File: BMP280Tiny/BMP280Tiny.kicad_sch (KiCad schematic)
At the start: 3 parts, among them J1 Programming Port, U1 ATtiny88-A, U2 AMS1117-5.0

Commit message: work on new vario board
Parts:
- removed U1: ATtiny88-A, Package_QFP:TQFP-32_7x7mm_P0.8mm, symbol MCU_Microchip_ATtiny:ATtiny88-A
- added C1: 0.1uF, Capacitor_SMD:C_0603_1608Metric_Pad1.08x0.95mm_HandSolder, symbol Device:C
- added J2: 9V Battery, Connector_Molex:Molex_KK-254_AE-6410-02A_1x02_P2.54mm_Vertical, symbol Connector_Generic:Conn_01x02
- added U1: ATtiny88-A, Package_QFP:TQFP-32_7x7mm_P0.8mm, symbol Project Library:ATtiny88-A
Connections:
- net GND: now reaches U2.1 (GND)
- net GND: now also C1.1, J2.1 (Pin_1)
- net 5V: now reaches U2.2 (VO)
- net at U2.3 (VI): now also C1.2, J2.2 (Pin_2)

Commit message: work on attiny88 board schematic
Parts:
- added C2, C3: 0.1uF, Capacitor_SMD:C_0603_1608Metric_Pad1.08x0.95mm_HandSolder, symbol Device:C
- added D1, D2: LED, symbol Device:LED
- added J3: Piezo Buzzer, Connector_Molex:Molex_KK-254_AE-6410-02A_1x02_P2.54mm_Vertical, symbol Connector_Generic:Conn_01x02
- added R1, R2, R3: R, symbol Device:R
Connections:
- net 5V: now also J1.2 (Pin_2), U1.18 (AVCC), U1.4 (VCC), C2.2, C3.2, R1.1
- net GND: now also J1.6 (Pin_6), U1.21 (GND), U1.5 (GND), C2.1, C3.1, D1.1 (K), D2.1 (K)
- net at U1.12 (PB0): now also R3.1
- net at U1.13 (PB1): now also J3.2 (Pin_2)
- net at U1.14 (PB2): now also J3.1 (Pin_1)
- net at U1.15 (PB3): now also J1.4 (Pin_4)
- net at U1.16 (PB4): now also J1.1 (Pin_1)
- net at U1.17 (PB5): now also J1.3 (Pin_3), R2.1
- net at U1.29 (~{RESET}/PC6): now also J1.5 (Pin_5), R1.2
- new net: D2.2 (A), R3.2
- new net: D1.2 (A), R2.2
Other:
- moved on the sheet: J1

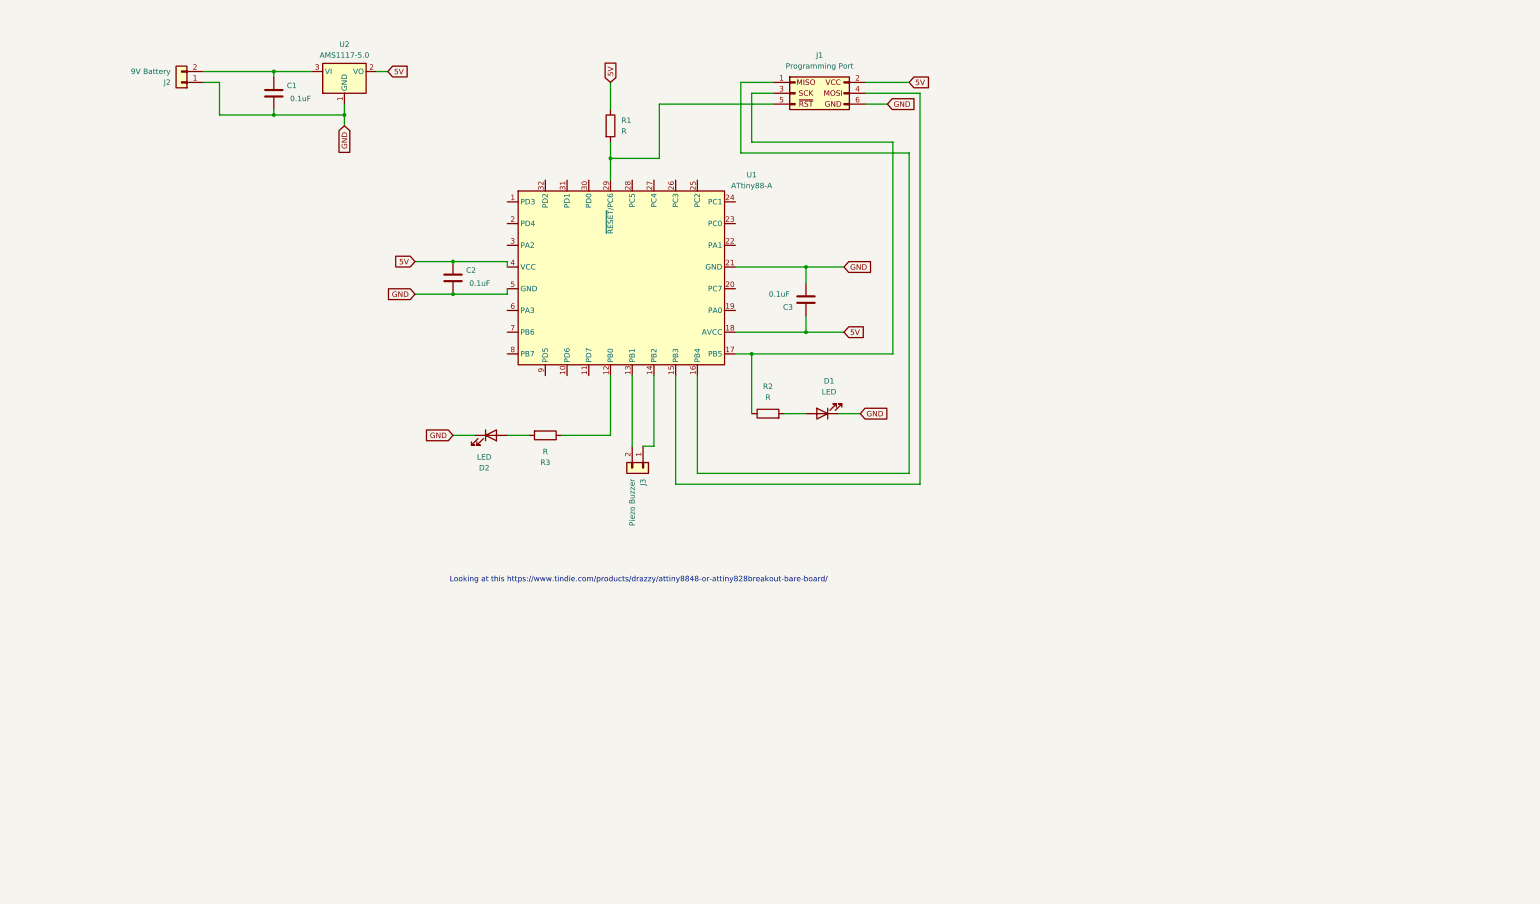
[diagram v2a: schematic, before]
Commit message: Vario v5 sent to jlcpcb for production
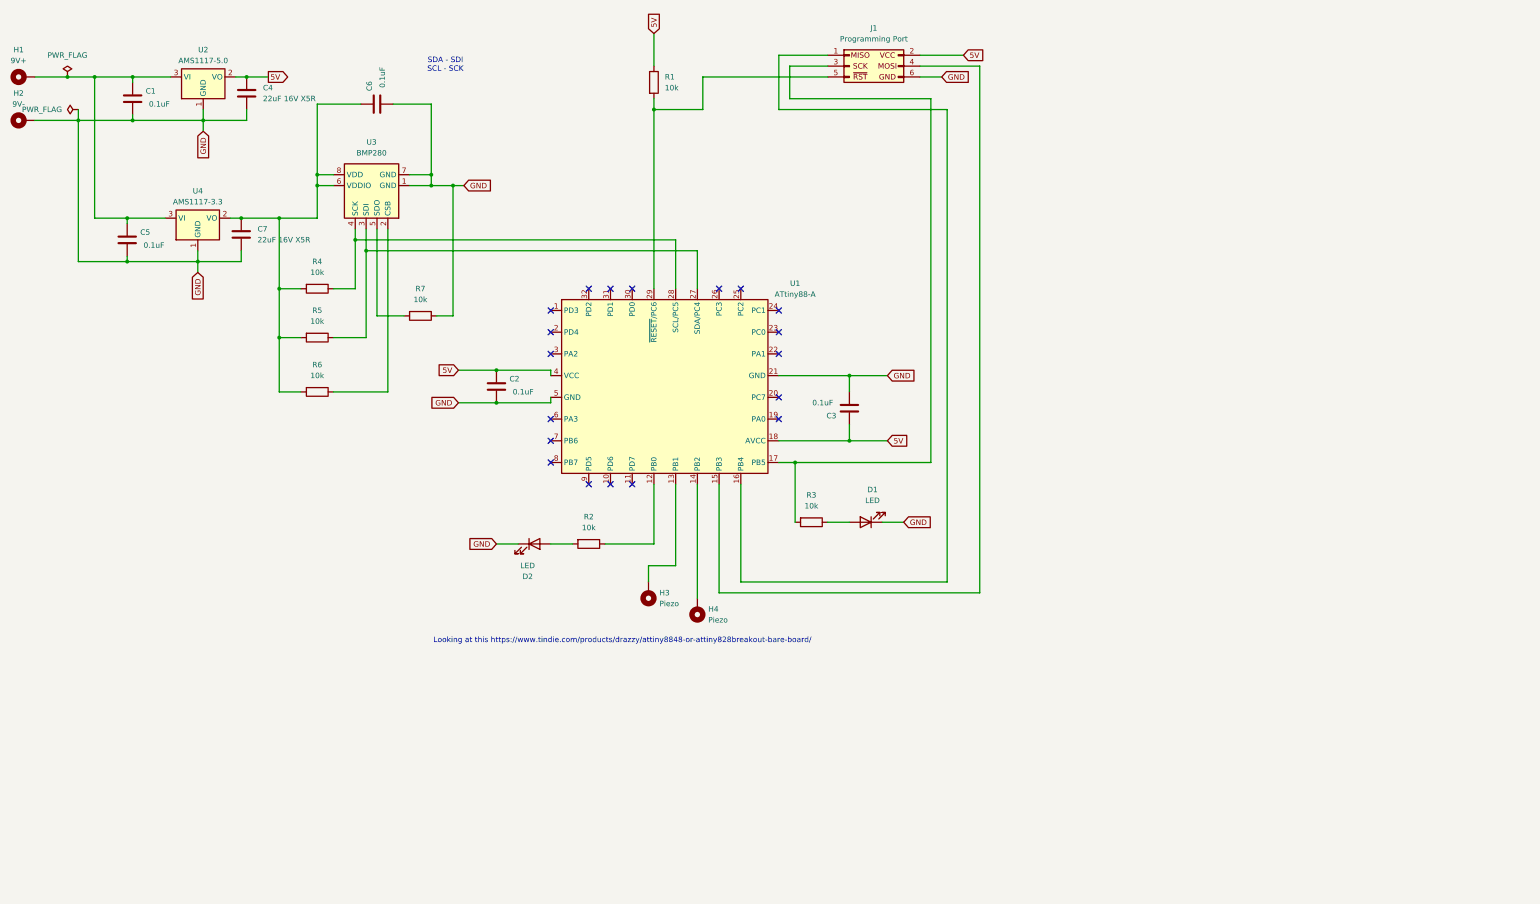
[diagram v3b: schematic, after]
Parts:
- removed J2: 9V Battery, Connector_Molex:Molex_KK-254_AE-6410-02A_1x02_P2.54mm_Vertical, symbol Connector_Generic:Conn_01x02
- removed J3: Piezo Buzzer, Connector_Molex:Molex_KK-254_AE-6410-02A_1x02_P2.54mm_Vertical, symbol Connector_Generic:Conn_01x02
- added C4, C7: 22uF 16V X5R, Capacitor_SMD:C_0805_2012Metric_Pad1.18x1.45mm_HandSolder, symbol Device:C
- added C5, C6: 0.1uF, Capacitor_SMD:C_0603_1608Metric_Pad1.08x0.95mm_HandSolder, symbol Device:C
- added H1: 9V+, TestPoint:TestPoint_THTPad_2.0x2.0mm_Drill1.0mm, symbol Mechanical:MountingHole_Pad
- added H2: 9V-, TestPoint:TestPoint_THTPad_2.0x2.0mm_Drill1.0mm, symbol Mechanical:MountingHole_Pad
- added H3, H4: Piezo, TestPoint:TestPoint_THTPad_2.0x2.0mm_Drill1.0mm, symbol Mechanical:MountingHole_Pad
- added R4, R5, R6, R7: 10k, Resistor_SMD:R_0603_1608Metric_Pad0.98x0.95mm_HandSolder, symbol Device:R
- added U3: BMP280, Library:Bosch_LGA-8_2x2.5mm_P0.65mm_ClockwisePinNumbering, symbol Sensor_Pressure:BMP280
- added U4: AMS1117-3.3, Package_TO_SOT_SMD:SOT-223-3_TabPin2, symbol Regulator_Linear:AMS1117-5.0
- D1, D2: footprint (none) -> LED_SMD:LED_0603_1608Metric_Pad1.05x0.95mm_HandSolder
- R1, R2, R3: value R -> 10k; footprint (none) -> Resistor_SMD:R_0603_1608Metric_Pad0.98x0.95mm_HandSolder
- U1: LCSC Part # (none) -> C111451
- U2: LCSC Part # (none) -> C6187
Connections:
- net 5V: now also C4.1
- net GND: now also C4.2, C5.1, C6.1, C7.2, H2.1, R7.1, U3.1 (GND), U3.7 (GND), U4.1 (GND)
- net at D2.2 (A): now also R2.2; no longer R3.2
- net at D1.2 (A): now also R3.1; no longer R2.2
- net at U1.12 (PB0): now also R2.1; no longer R3.1
- net at U1.13 (PB1): now also H3.1
- net at U1.14 (PB2): now also H4.1
- net at J1.3 (Pin_3), U1.17 (PB5): now also R3.2; no longer R2.1
- net at U1.27 (SDA/PC4): now also R5.1, U3.3 (SDI)
- net at U1.28 (SCL/PC5): now also R4.1, U3.4 (SCK)
- net at C1.2, U2.3 (VI): now also C5.2, H1.1, U4.3 (VI)
- new net: R6.1, U3.2 (CSB)
- new net: R7.2, U3.5 (SDO)
- new net: C6.2, C7.1, R4.2, R5.2, R6.2, U3.6 (VDDIO), U3.8 (VDD), U4.2 (VO)
- no-connect marks 0 -> 19
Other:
- note added: "SDA - SDI SCL - SCK"
- moved on the sheet: C1, C2, C3, D1, D2, J1, U1, U2

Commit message: work on vario board
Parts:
- removed C1, C5: 0.1uF, Capacitor_SMD:C_0603_1608Metric_Pad1.08x0.95mm_HandSolder, symbol Device:C
- removed C4, C7: 22uF 16V X5R, Capacitor_SMD:C_0805_2012Metric_Pad1.18x1.45mm_HandSolder, symbol Device:C
- removed D1: LED, LED_SMD:LED_0603_1608Metric_Pad1.05x0.95mm_HandSolder, symbol Device:LED
- removed R3: 10k, Resistor_SMD:R_0603_1608Metric_Pad0.98x0.95mm_HandSolder, symbol Device:R
- removed U2: AMS1117-5.0, Package_TO_SOT_SMD:SOT-223-3_TabPin2, symbol Regulator_Linear:AMS1117-5.0
- removed U4: AMS1117-3.3, Package_TO_SOT_SMD:SOT-223-3_TabPin2, symbol Regulator_Linear:AMS1117-5.0
- added C10, C15: 0.1uF, Capacitor_SMD:C_0603_1608Metric_Pad1.08x0.95mm_HandSolder, symbol Device:C
- added C11, C12, C16, C17: 22uF 16V X5R, Capacitor_SMD:C_0805_2012Metric_Pad1.18x1.45mm_HandSolder, symbol Device:C
- added C13, C8: 10nF, Capacitor_SMD:C_0603_1608Metric_Pad1.08x0.95mm_HandSolder, symbol Device:C
- added C14, C9: 2.2uF 50V X5R, Capacitor_SMD:C_0805_2012Metric_Pad1.18x1.45mm_HandSolder, symbol Device:C
- added L1: 6.8uH, Library:L_Abracon_ASPI-0310FS, symbol Device:L
- added L2: 5.6uH, Library:L_Abracon_ASPI-0310FS, symbol Device:L
- added R10, R8: 100k, Resistor_SMD:R_0603_1608Metric_Pad0.98x0.95mm_HandSolder, symbol Device:R
- added R11: 22.1k, Resistor_SMD:R_0805_2012Metric_Pad1.20x1.40mm_HandSolder, symbol Device:R
- added R9: 13.7k, Resistor_SMD:R_0805_2012Metric_Pad1.20x1.40mm_HandSolder, symbol Device:R
- added SW1: SW_DPST_x2, Library:SW_19x12, symbol Switch:SW_DPST_x2
- added U5, U6: LMR51430, Package_TO_SOT_SMD:SOT-23-6_Handsoldering, symbol PowerLibrary:LMR51430
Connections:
- net 5V: now also C11.1, C12.1, L1.2, R8.1
- net GND: now also C11.2, C12.2, C13.2, C14.2, C16.2, C17.2, C8.2, C9.2, R11.2, R9.2, U5.1 (GND), U6.1 (GND)
- net 3.3V: now reaches C6.2, R4.2, R5.2, R6.2, U3.6 (VDDIO), U3.8 (VDD)
- net 3.3V: now also C16.1, C17.1, L2.2, R10.1
- net VIN: now reaches H1.1
- net VIN: now also SW1.1 (A)
- new net: C15.1, U6.6 (CB)
- new net: C15.2, L2.1, U6.2 (SW)
- new net: R10.2, R11.1, U6.4 (FB)
- new net: R8.2, R9.1, U5.4 (FB)
- new net: C10.2, L1.1, U5.2 (SW)
- new net: C10.1, U5.6 (CB)
- new net: C13.1, C14.1, C8.1, C9.1, SW1.2 (B), U5.3 (VIN), U5.5 (EN), U6.3 (VIN), U6.5 (EN)
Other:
- moved on the sheet: C2, C3, C6, D2, H1, H2, H3, H4, J1, R1, R2, R4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
